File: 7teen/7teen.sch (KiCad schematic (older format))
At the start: 18 parts

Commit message: [keyboard] 7teen: schematic development
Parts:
- removed SW?: SW_Push, symbol Switch:SW_Push
- added D_A0, D_A1, D_A2, D_A3, D_B0, D_B1, D_B2, D_B3, D_C0, D_C1, D_C2, D_C3, D_C4, D_D0, D_D1, D_D2, D_D4: D_Small, symbol Device:D_Small
- added SwC4: Rotary_Encoder_Switch, keebio:RotaryEncoder_EC11, symbol Device:Rotary_Encoder_Switch
- U0: renamed from U?; footprint (none) -> keeblib:Seeeduino_XIAO-MOUDLE14P-2.54-21X17.8MM
- gave numbers to parts that had none: 16
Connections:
- net row0 is gone; now on net rowA: U0.11 (PA6_A10_D10_MOSI)
- net row1 is gone; now on net rowB: U0.10 (PA5_A9_D9_MISO)
- net row2 is gone; now on net rowC: U0.9 (PA7_A8_D8_SCK)
- net row3 is gone; now on net rowD: U0.8 (PB09_A7_D7_RX)
- net col4: now also SwC4.S2
- net encA: now also SwC4.A
- net encB: now also SwC4.B
- net rowA: now also D_A0.1 (K), D_A1.1 (K), D_A2.1 (K), D_A3.1 (K); no longer SwA0.1, SwA1.1, SwA2.1, SwA3.1
- net rowB: now also D_B0.1 (K), D_B1.1 (K), D_B2.1 (K), D_B3.1 (K); no longer SwB0.1, SwB1.1, SwB2.1, SwB3.1
- net rowC: now also D_C0.1 (K), D_C1.1 (K), D_C2.1 (K), D_C3.1 (K), D_C4.1 (K); no longer SwC0.1, SwC1.1, SwC2.1, SwC3.1
- net rowD: now also D_D0.1 (K), D_D1.1 (K), D_D2.1 (K), D_D4.1 (K); no longer SwD0.1, SwD1.1, SwD2.1, SwD4.1
- net GND: now reaches U0.13 (GND)
- net GND: now also SwC4.C
- new net: D_A0.2 (A), SwA0.1
- new net: D_A1.2 (A), SwA1.1
- new net: D_A2.2 (A), SwA2.1
- new net: D_A3.2 (A), SwA3.1
- new net: D_C4.2 (A), SwC4.S1
- new net: D_B0.2 (A), SwB0.1
- new net: D_B1.2 (A), SwB1.1
- new net: D_B2.2 (A), SwB2.1
- new net: D_B3.2 (A), SwB3.1
- new net: D_C0.2 (A), SwC0.1
- new net: D_C1.2 (A), SwC1.1
- new net: D_C2.2 (A), SwC2.1
- new net: D_C3.2 (A), SwC3.1
- new net: D_D0.2 (A), SwD0.1
- new net: D_D1.2 (A), SwD1.1
- new net: D_D2.2 (A), SwD2.1
- new net: D_D4.2 (A), SwD4.1
- no-connect marks 0 -> 8
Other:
- moved on the sheet: SwB0, SwB1, SwB2, SwB3, SwC0, SwC1, SwC2, SwC3, SwD0, SwD1, SwD2, SwD4

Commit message: [keyboard] 7teen: schematic & pcb development
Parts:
- D_A0, D_A1, D_A2, D_A3, D_B0, D_B1, D_B2, D_B3, D_C0, D_C1, D_C2, D_C3, D_C4, D_D0, D_D1, D_D2, D_D4: footprint (none) -> keeblib:D_MiniMELF_bsides
- SwA0, SwA1, SwA2, SwA3, SwB0, SwB1, SwB2, SwB3, SwC0, SwC1, SwC2, SwC3, SwD0, SwD1, SwD2, SwD4: footprint (none) -> keeblib:pg1353_dual
- U0: footprint keeblib:Seeeduino_XIAO-MOUDLE14P-2.54-21X17.8MM -> keeblib:Seeeduino_XIAO_dual
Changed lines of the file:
@@
 F 0 "U0" H 8775 1561 50  0000 C CNN
 F 1 "SeeeduinoXIAO" H 8775 1470 50  0000 C CNN
-F 2 "keeblib:Seeeduino_XIAO-MOUDLE14P-2.54-21X17.8MM" H 8450 2700 50  0001 C CNN
+F 2 "keeblib:Seeeduino_XIAO_dual" H 8450 2700 50  0001 C CNN
 F 3 "" H 8450 2700 50  0001 C CNN
 	1    8800 2500
@@
 F 0 "SwA0" H 2100 3285 50  0000 C CNN
 F 1 "SW_Push" H 2100 3194 50  0000 C CNN
-F 2 "" H 2100 3200 50  0001 C CNN
+F 2 "keeblib:pg1353_dual" H 2100 3200 50  0001 C CNN
 F 3 "~" H 2100 3200 50  0001 C CNN
 	1    2100 3000
@@
 F 0 "SwA1" H 2600 3285 50  0000 C CNN
 F 1 "SW_Push" H 2600 3194 50  0000 C CNN
-F 2 "" H 2600 3200 50  0001 C CNN
+F 2 "keeblib:pg1353_dual" H 2600 3200 50  0001 C CNN
 F 3 "~" H 2600 3200 50  0001 C CNN
 	1    2600 3000
@@
 F 0 "SwA2" H 3100 3285 50  0000 C CNN
 F 1 "SW_Push" H 3100 3194 50  0000 C CNN
-F 2 "" H 3100 3200 50  0001 C CNN
+F 2 "keeblib:pg1353_dual" H 3100 3200 50  0001 C CNN
 F 3 "~" H 3100 3200 50  0001 C CNN
 	1    3100 3000
@@
 F 0 "SwA3" H 3600 3285 50  0000 C CNN
 F 1 "SW_Push" H 3600 3194 50  0000 C CNN
-F 2 "" H 3600 3200 50  0001 C CNN
+F 2 "keeblib:pg1353_dual" H 3600 3200 50  0001 C CNN
 F 3 "~" H 3600 3200 50  0001 C CNN
 	1    3600 3000
@@
 F 0 "SwB0" H 2100 3885 50  0000 C CNN
 F 1 "SW_Push" H 2100 3794 50  0000 C CNN
-F 2 "" H 2100 3800 50  0001 C CNN
+F 2 "keeblib:pg1353_dual" H 2100 3800 50  0001 C CNN
 F 3 "~" H 2100 3800 50  0001 C CNN
 	1    2100 3600
@@
 F 0 "SwB1" H 2600 3885 50  0000 C CNN
 F 1 "SW_Push" H 2600 3794 50  0000 C CNN
-F 2 "" H 2600 3800 50  0001 C CNN
+F 2 "keeblib:pg1353_dual" H 2600 3800 50  0001 C CNN
 F 3 "~" H 2600 3800 50  0001 C CNN
 	1    2600 3600
@@
 F 0 "SwB2" H 3100 3885 50  0000 C CNN
 F 1 "SW_Push" H 3100 3794 50  0000 C CNN
-F 2 "" H 3100 3800 50  0001 C CNN
+F 2 "keeblib:pg1353_dual" H 3100 3800 50  0001 C CNN
 F 3 "~" H 3100 3800 50  0001 C CNN
 	1    3100 3600
@@
 F 0 "SwB3" H 3600 3885 50  0000 C CNN
 F 1 "SW_Push" H 3600 3794 50  0000 C CNN
-F 2 "" H 3600 3800 50  0001 C CNN
+F 2 "keeblib:pg1353_dual" H 3600 3800 50  0001 C CNN
 F 3 "~" H 3600 3800 50  0001 C CNN
 	1    3600 3600
@@
 F 0 "SwC0" H 2100 4485 50  0000 C CNN
 F 1 "SW_Push" H 2100 4394 50  0000 C CNN
-F 2 "" H 2100 4400 50  0001 C CNN
+F 2 "keeblib:pg1353_dual" H 2100 4400 50  0001 C CNN
 F 3 "~" H 2100 4400 50  0001 C CNN
 	1    2100 4200
@@
 F 0 "SwC1" H 2600 4485 50  0000 C CNN
 F 1 "SW_Push" H 2600 4394 50  0000 C CNN
-F 2 "" H 2600 4400 50  0001 C CNN
+F 2 "keeblib:pg1353_dual" H 2600 4400 50  0001 C CNN
 F 3 "~" H 2600 4400 50  0001 C CNN
 	1    2600 4200
@@
 F 0 "SwC2" H 3100 4485 50  0000 C CNN
 F 1 "SW_Push" H 3100 4394 50  0000 C CNN
-F 2 "" H 3100 4400 50  0001 C CNN
+F 2 "keeblib:pg1353_dual" H 3100 4400 50  0001 C CNN
 F 3 "~" H 3100 4400 50  0001 C CNN
 	1    3100 4200
@@
 F 0 "SwC3" H 3600 4485 50  0000 C CNN
 F 1 "SW_Push" H 3600 4394 50  0000 C CNN
-F 2 "" H 3600 4400 50  0001 C CNN
+F 2 "keeblib:pg1353_dual" H 3600 4400 50  0001 C CNN
 F 3 "~" H 3600 4400 50  0001 C CNN
 	1    3600 4200
@@
 F 0 "SwD0" H 2100 5085 50  0000 C CNN
 F 1 "SW_Push" H 2100 4994 50  0000 C CNN
-F 2 "" H 2100 5000 50  0001 C CNN
+F 2 "keeblib:pg1353_dual" H 2100 5000 50  0001 C CNN
 F 3 "~" H 2100 5000 50  0001 C CNN
 	1    2100 4800
@@
 F 0 "SwD1" H 2600 5085 50  0000 C CNN
 F 1 "SW_Push" H 2600 4994 50  0000 C CNN
-F 2 "" H 2600 5000 50  0001 C CNN
+F 2 "keeblib:pg1353_dual" H 2600 5000 50  0001 C CNN
 F 3 "~" H 2600 5000 50  0001 C CNN
 	1    2600 4800
@@
 F 0 "SwD2" H 3100 5085 50  0000 C CNN
 F 1 "SW_Push" H 3100 4994 50  0000 C CNN
-F 2 "" H 3100 5000 50  0001 C CNN
+F 2 "keeblib:pg1353_dual" H 3100 5000 50  0001 C CNN
 F 3 "~" H 3100 5000 50  0001 C CNN
 	1    3100 4800
-	1    0    0    -1
-$EndComp
-$Comp
-L Switch:SW_Push SwD4
-U 1 1 60A9A1CE
-P 3850 4800
-F 0 "SwD4" H 3850 5085 50  0000 C CNN
-F 1 "SW_Push" H 3850 4994 50  0000 C CNN
-F 2 "" H 3850 5000 50  0001 C CNN
-F 3 "~" H 3850 5000 50  0001 C CNN
-	1    3850 4800
 	1    0    0    -1
 $EndComp
@@
 F 0 "D_A0" V 1946 3030 50  0000 R CNN
 F 1 "D_Small" V 1855 3030 50  0000 R CNN
-F 2 "" V 1900 3100 50  0001 C CNN
+F 2 "keeblib:D_MiniMELF_bsides" V 1900 3100 50  0001 C CNN
 F 3 "~" V 1900 3100 50  0001 C CNN
 	1    1900 3100
@@
 F 0 "D_A1" V 2446 3030 50  0000 R CNN
 F 1 "D_Small" V 2355 3030 50  0000 R CNN
-F 2 "" V 2400 3100 50  0001 C CNN
+F 2 "keeblib:D_MiniMELF_bsides" V 2400 3100 50  0001 C CNN
 F 3 "~" V 2400 3100 50  0001 C CNN
 	1    2400 3100
@@
 F 0 "D_A2" V 2946 3030 50  0000 R CNN
 F 1 "D_Small" V 2855 3030 50  0000 R CNN
-F 2 "" V 2900 3100 50  0001 C CNN
+F 2 "keeblib:D_MiniMELF_bsides" V 2900 3100 50  0001 C CNN
 F 3 "~" V 2900 3100 50  0001 C CNN
 	1    2900 3100
@@
 F 0 "D_A3" V 3446 3030 50  0000 R CNN
 F 1 "D_Small" V 3355 3030 50  0000 R CNN
-F 2 "" V 3400 3100 50  0001 C CNN
+F 2 "keeblib:D_MiniMELF_bsides" V 3400 3100 50  0001 C CNN
 F 3 "~" V 3400 3100 50  0001 C CNN
 	1    3400 3100
@@
 F 0 "D_B0" V 1946 3630 50  0000 R CNN
 F 1 "D_Small" V 1855 3630 50  0000 R CNN
-F 2 "" V 1900 3700 50  0001 C CNN
+F 2 "keeblib:D_MiniMELF_bsides" V 1900 3700 50  0001 C CNN
 F 3 "~" V 1900 3700 50  0001 C CNN
 	1    1900 3700
@@
 F 0 "D_B1" V 2446 3630 50  0000 R CNN
 F 1 "D_Small" V 2355 3630 50  0000 R CNN
-F 2 "" V 2400 3700 50  0001 C CNN
+F 2 "keeblib:D_MiniMELF_bsides" V 2400 3700 50  0001 C CNN
 F 3 "~" V 2400 3700 50  0001 C CNN
 	1    2400 3700
@@
 F 0 "D_B2" V 2946 3630 50  0000 R CNN
 F 1 "D_Small" V 2855 3630 50  0000 R CNN
-F 2 "" V 2900 3700 50  0001 C CNN
+F 2 "keeblib:D_MiniMELF_bsides" V 2900 3700 50  0001 C CNN
 F 3 "~" V 2900 3700 50  0001 C CNN
 	1    2900 3700
@@
 F 0 "D_B3" V 3446 3630 50  0000 R CNN
 F 1 "D_Small" V 3355 3630 50  0000 R CNN
-F 2 "" V 3400 3700 50  0001 C CNN
+F 2 "keeblib:D_MiniMELF_bsides" V 3400 3700 50  0001 C CNN
 F 3 "~" V 3400 3700 50  0001 C CNN
 	1    3400 3700
@@
 F 0 "D_C0" V 1946 4230 50  0000 R CNN
 F 1 "D_Small" V 1855 4230 50  0000 R CNN
-F 2 "" V 1900 4300 50  0001 C CNN
+F 2 "keeblib:D_MiniMELF_bsides" V 1900 4300 50  0001 C CNN
 F 3 "~" V 1900 4300 50  0001 C CNN
 	1    1900 4300
@@
 F 0 "D_C1" V 2446 4230 50  0000 R CNN
 F 1 "D_Small" V 2355 4230 50  0000 R CNN
-F 2 "" V 2400 4300 50  0001 C CNN
+F 2 "keeblib:D_MiniMELF_bsides" V 2400 4300 50  0001 C CNN
 F 3 "~" V 2400 4300 50  0001 C CNN
 	1    2400 4300
@@
 F 0 "D_C2" V 2946 4230 50  0000 R CNN
 F 1 "D_Small" V 2855 4230 50  0000 R CNN
-F 2 "" V 2900 4300 50  0001 C CNN
+F 2 "keeblib:D_MiniMELF_bsides" V 2900 4300 50  0001 C CNN
 F 3 "~" V 2900 4300 50  0001 C CNN
 	1    2900 4300
@@
 F 0 "D_C3" V 3446 4230 50  0000 R CNN
 F 1 "D_Small" V 3355 4230 50  0000 R CNN
-F 2 "" V 3400 4300 50  0001 C CNN
+F 2 "keeblib:D_MiniMELF_bsides" V 3400 4300 50  0001 C CNN
 F 3 "~" V 3400 4300 50  0001 C CNN
 	1    3400 4300
@@
 F 0 "D_C4" H 3950 4607 50  0000 C CNN
 F 1 "D_Small" H 3950 4516 50  0000 C CNN
-F 2 "" V 3950 4400 50  0001 C CNN
+F 2 "keeblib:D_MiniMELF_bsides" V 3950 4400 50  0001 C CNN
 F 3 "~" V 3950 4400 50  0001 C CNN
 	1    3950 4400
@@
 Connection ~ 3400 4400
 Connection ~ 4050 4200
-Wire Wire Line
-	4050 4200 4050 4800
 Wire Wire Line
 	4900 4300 4650 4300
@@
 F 0 "D_D0" V 1946 4830 50  0000 R CNN
 F 1 "D_Small" V 1855 4830 50  0000 R CNN
-F 2 "" V 1900 4900 50  0001 C CNN
+F 2 "keeblib:D_MiniMELF_bsides" V 1900 4900 50  0001 C CNN
 F 3 "~" V 1900 4900 50  0001 C CNN
 	1    1900 4900
@@
 F 0 "D_D1" V 2446 4830 50  0000 R CNN
 F 1 "D_Small" V 2355 4830 50  0000 R CNN
-F 2 "" V 2400 4900 50  0001 C CNN
+F 2 "keeblib:D_MiniMELF_bsides" V 2400 4900 50  0001 C CNN
 F 3 "~" V 2400 4900 50  0001 C CNN
 	1    2400 4900
@@
 F 0 "D_D2" V 2946 4830 50  0000 R CNN
 F 1 "D_Small" V 2855 4830 50  0000 R CNN
-F 2 "" V 2900 4900 50  0001 C CNN
+F 2 "keeblib:D_MiniMELF_bsides" V 2900 4900 50  0001 C CNN
 F 3 "~" V 2900 4900 50  0001 C CNN
 	1    2900 4900
 	0    -1   -1   0
 $EndComp
-$Comp
-L Device:D_Small D_D4
-U 1 1 60B5942F
-P 3650 4900
-F 0 "D_D4" V 3696 4830 50  0000 R CNN
-F 1 "D_Small" V 3605 4830 50  0000 R CNN
-F 2 "" V 3650 4900 50  0001 C CNN
-F 3 "~" V 3650 4900 50  0001 C CNN
-	1    3650 4900
-	0    -1   -1   0
-$EndComp
 Connection ~ 1900 5000
 Wire Wire Line
@@
 Wire Wire Line
 	2900 5000 2400 5000
-Wire Wire Line
-	2900 5000 3650 5000
 $Comp
 L power:GND #PWR0104
@@
 	0    -1   -1   0
 $EndComp
+Wire Wire Line
+	4050 4200 4050 4800
+Wire Wire Line
+	2900 5000 3650 5000
+$Comp
+L Device:D_Small D_D4
+U 1 1 60B5942F
+P 3650 4900
+F 0 "D_D4" V 3696 4830 50  0000 R CNN
+F 1 "D_Small" V 3605 4830 50  0000 R CNN
+F 2 "keeblib:D_MiniMELF_bsides" V 3650 4900 50  0001 C CNN
+F 3 "~" V 3650 4900 50  0001 C CNN
+	1    3650 4900
+	0    -1   -1   0
+$EndComp
+$Comp
+L Switch:SW_Push SwD4
+U 1 1 60A9A1CE
+P 3850 4800
+F 0 "SwD4" H 3850 5085 50  0000 C CNN
+F 1 "SW_Push" H 3850 4994 50  0000 C CNN
+F 2 "keeblib:pg1353_dual" H 3850 5000 50  0001 C CNN
+F 3 "~" H 3850 5000 50  0001 C CNN
+	1    3850 4800
+	1    0    0    -1
+$EndComp
 $EndSCHEMATC

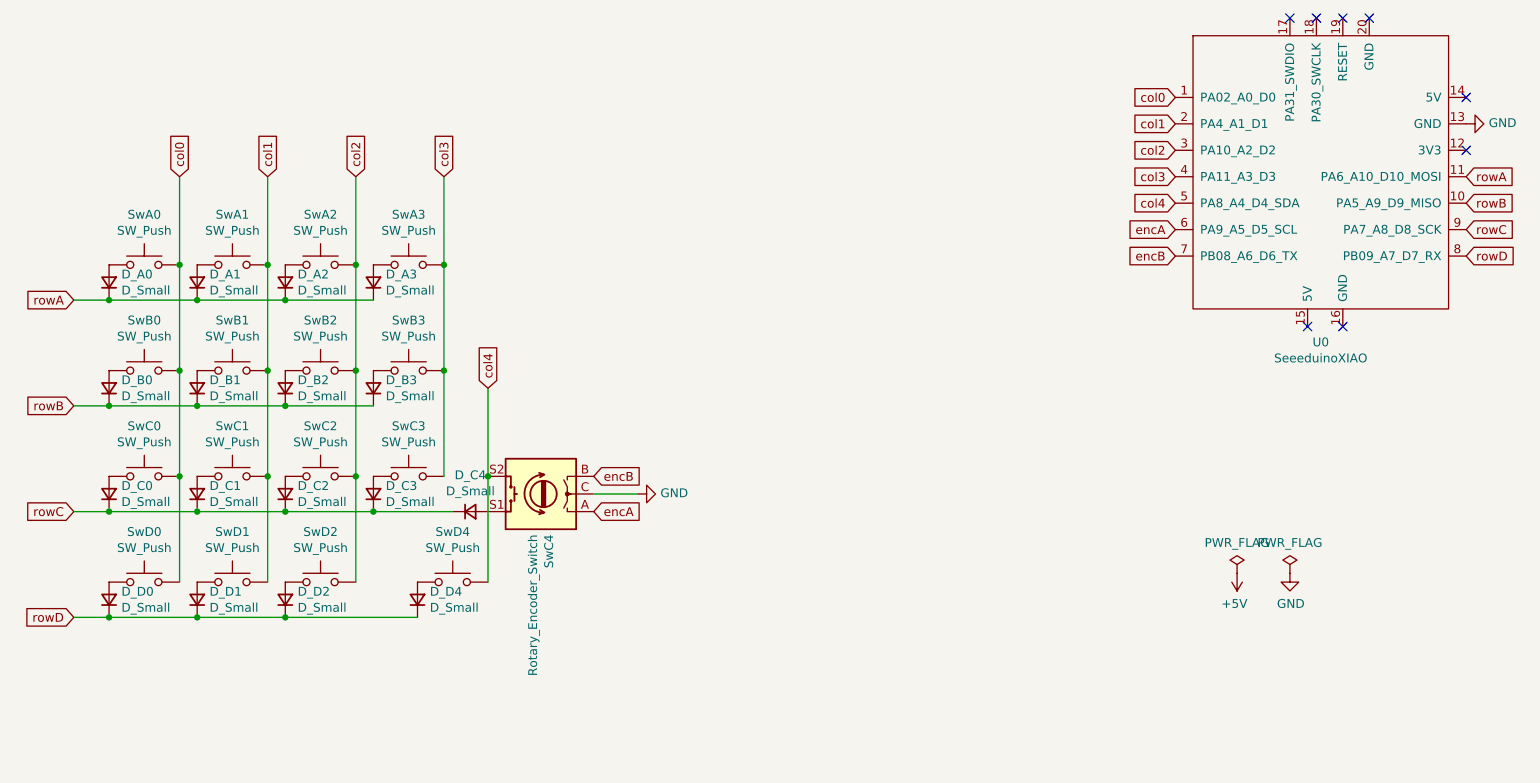
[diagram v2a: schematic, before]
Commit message: [keyboard] 7teen: pcb development
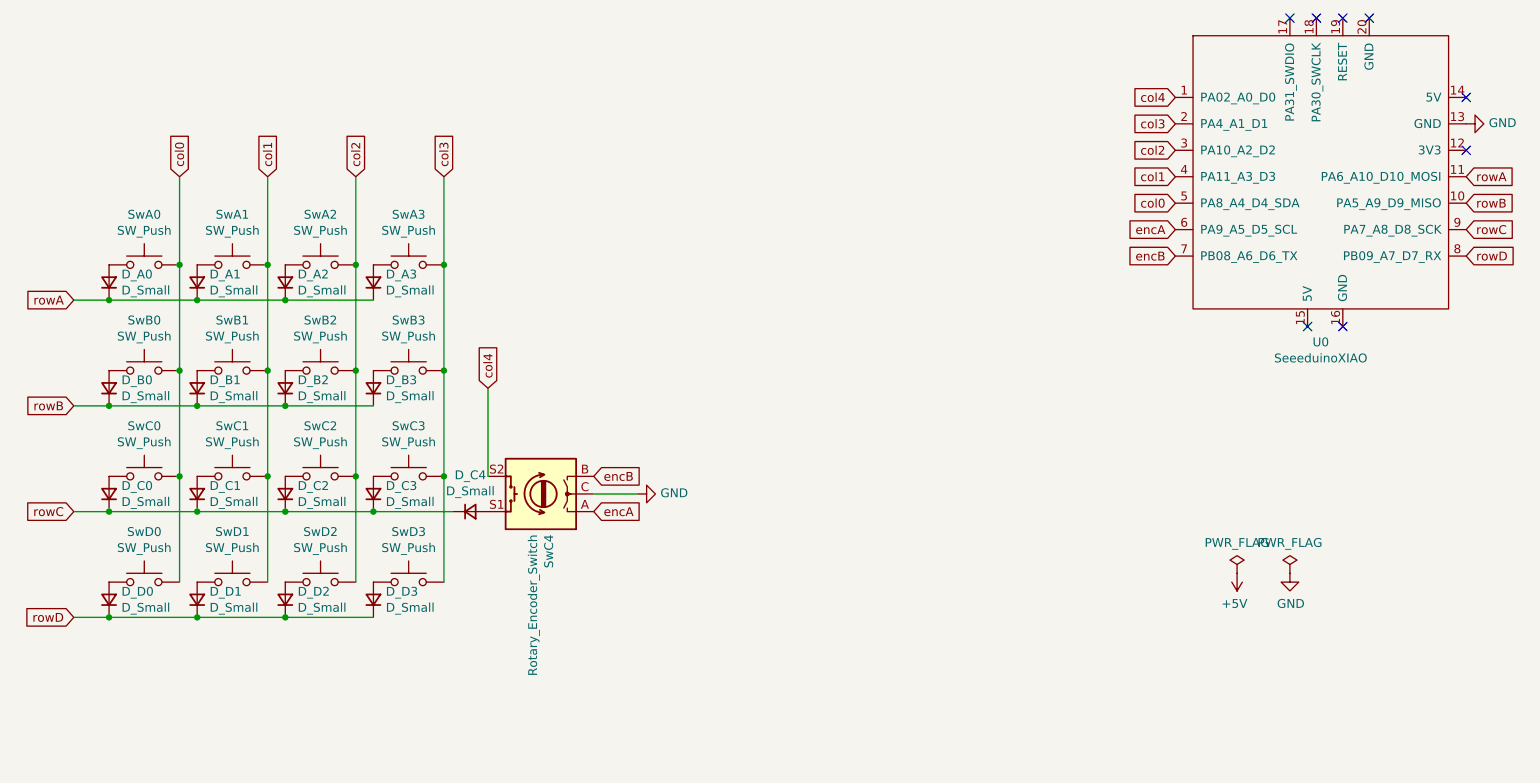
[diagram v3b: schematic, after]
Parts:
- U0: footprint keeblib:Seeeduino_XIAO_dual -> keeblib:Seeeduino_XIAO_dual_tht
- renumbered D_D4 to D_D3, SwD4 to SwD3
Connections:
- net col0: now also U0.5 (PA8_A4_D4_SDA); no longer U0.1 (PA02_A0_D0)
- net col1: now also U0.4 (PA11_A3_D3); no longer U0.2 (PA4_A1_D1)
- net col3: now also SwD3.2, U0.2 (PA4_A1_D1); no longer U0.4 (PA11_A3_D3)
- net col4: now also U0.1 (PA02_A0_D0); no longer SwD3.2, U0.5 (PA8_A4_D4_SDA)
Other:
- moved on the sheet: D_D3, SwD3

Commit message: [keyboard] 7teen:version update
Application of lessons-learned
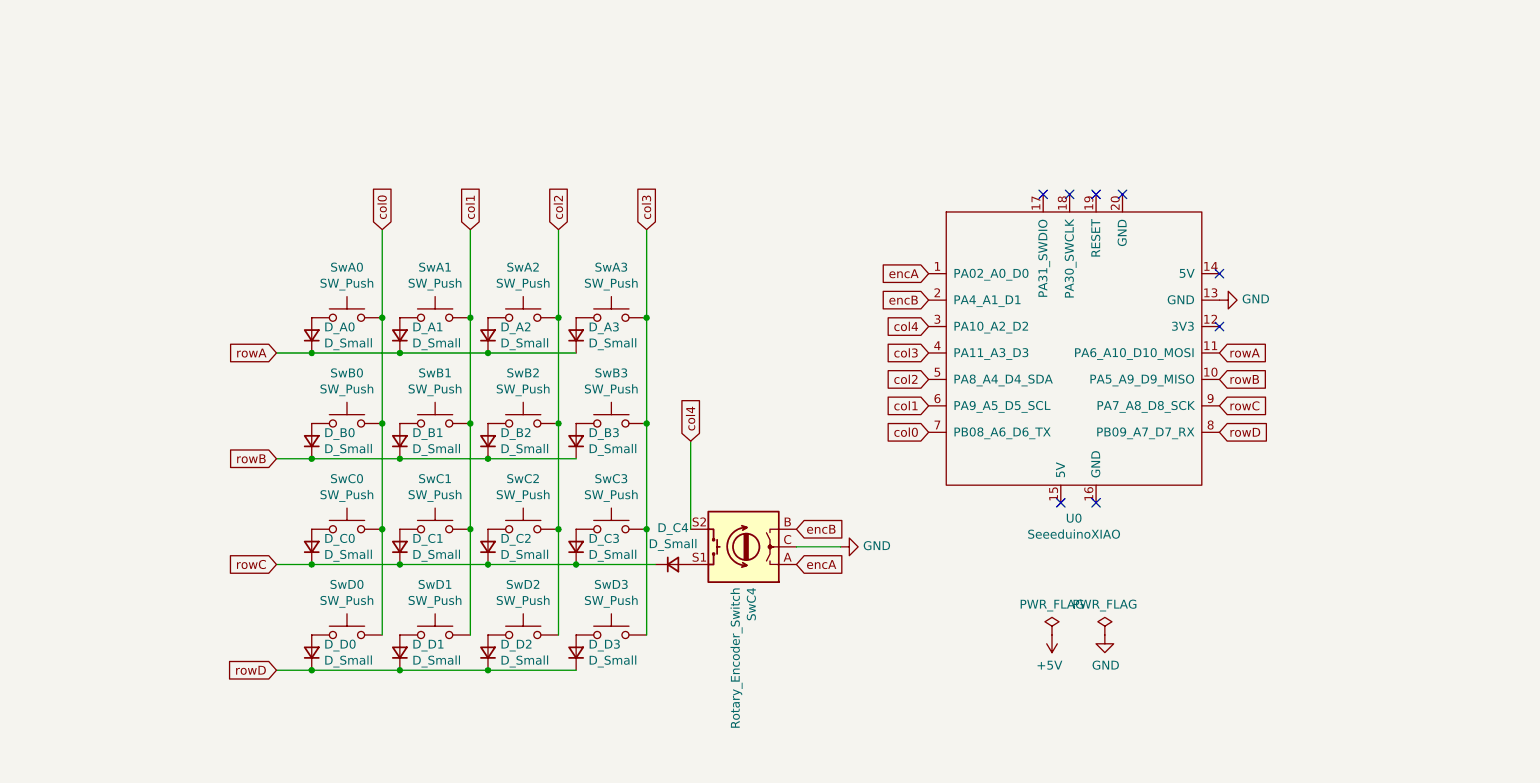
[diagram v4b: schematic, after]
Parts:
- SwD3: footprint keeblib:pg1353_dual -> keeblib:pg1353_reversible_2u
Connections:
- net col0: now also U0.7 (PB08_A6_D6_TX); no longer U0.5 (PA8_A4_D4_SDA)
- net col1: now also U0.6 (PA9_A5_D5_SCL); no longer U0.4 (PA11_A3_D3)
- net col2: now also U0.5 (PA8_A4_D4_SDA); no longer U0.3 (PA10_A2_D2)
- net col3: now also U0.4 (PA11_A3_D3); no longer U0.2 (PA4_A1_D1)
- net col4: now also U0.3 (PA10_A2_D2); no longer U0.1 (PA02_A0_D0)
- net encA: now also U0.1 (PA02_A0_D0); no longer U0.6 (PA9_A5_D5_SCL)
- net encB: now also U0.2 (PA4_A1_D1); no longer U0.7 (PB08_A6_D6_TX)
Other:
- moved on the sheet: D_A0, D_A1, D_A2, D_A3, D_B0, D_B1, D_B2, D_B3, D_C0, D_C1, D_C2, D_C3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
